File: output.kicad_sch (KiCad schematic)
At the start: 9 parts, among them Q3 NPN, Q4 PNP, U4 ${SIM.PARAMS}, U5 ${SIM.PARAMS}

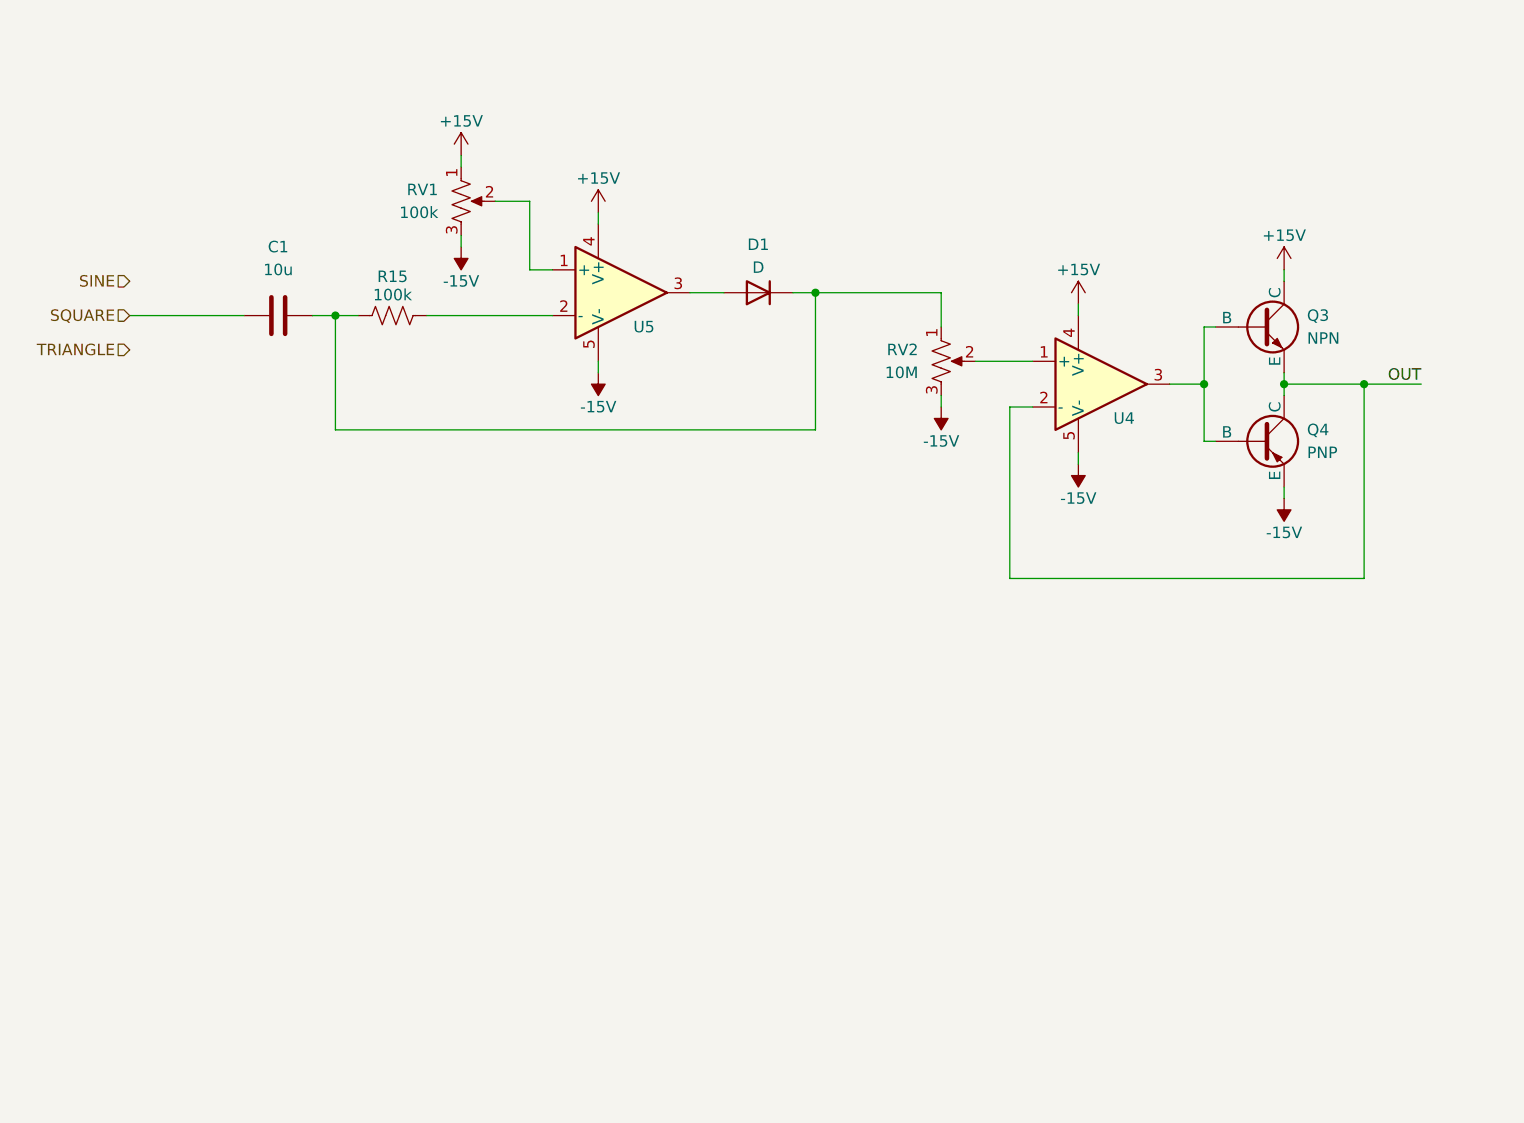
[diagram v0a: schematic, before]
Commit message: added spice model and reworked output stage
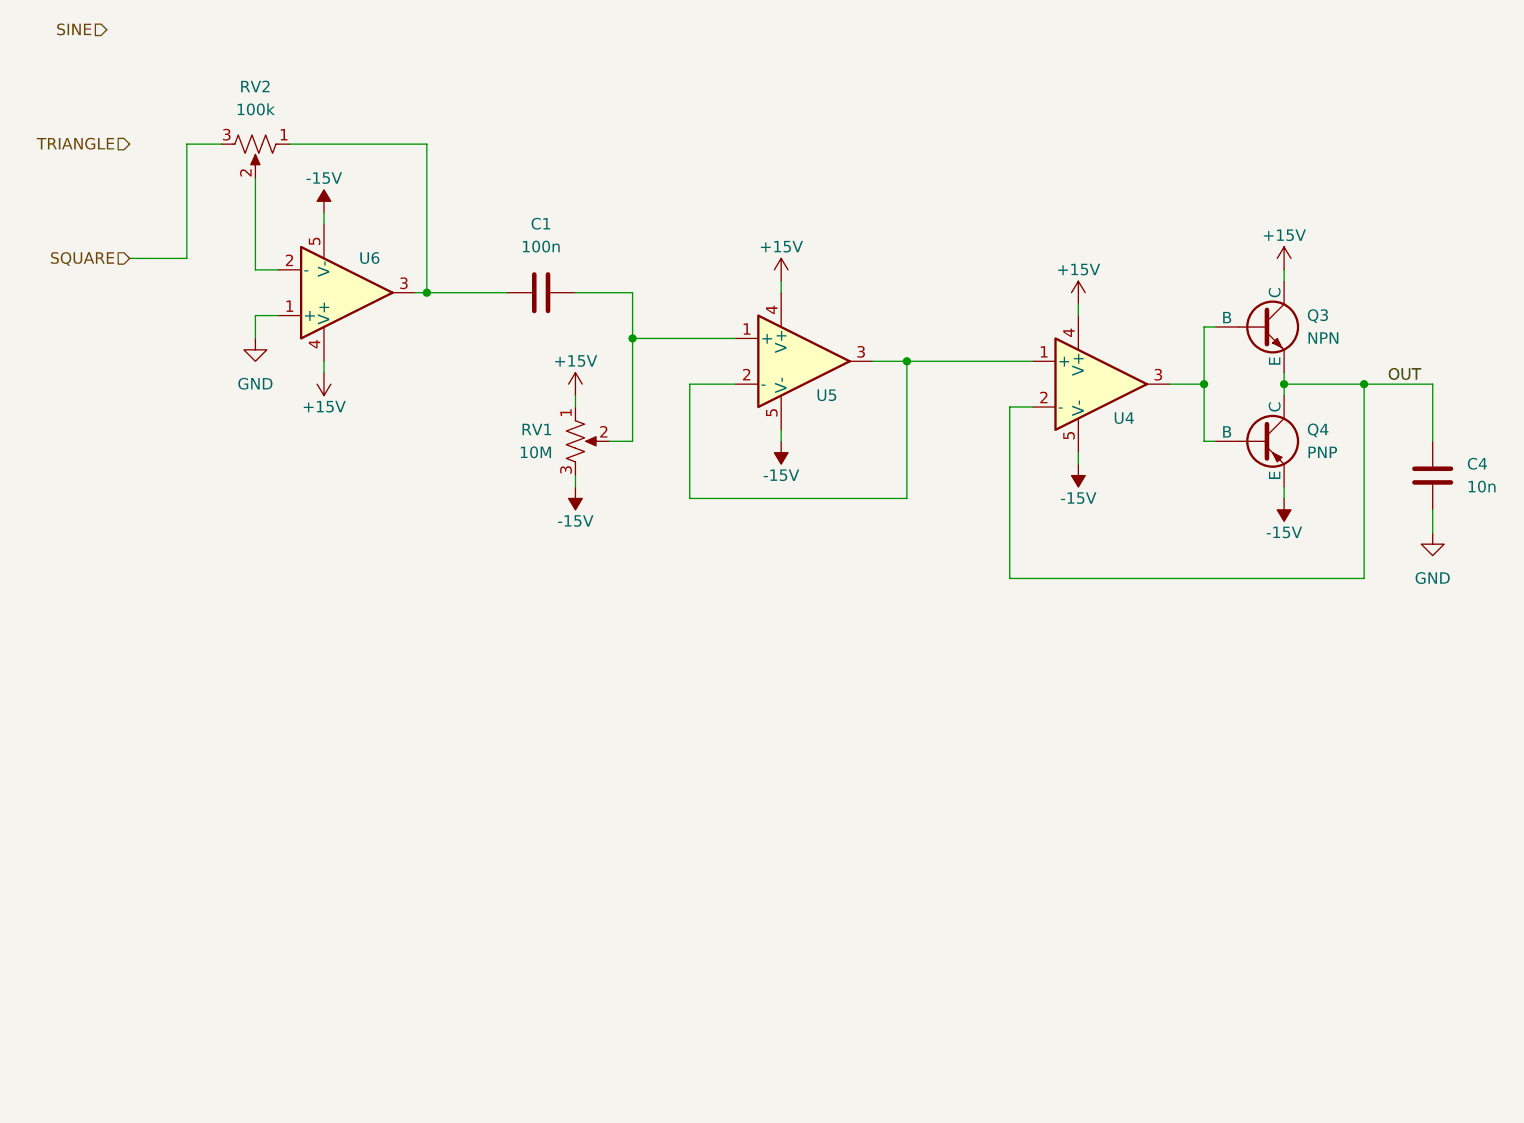
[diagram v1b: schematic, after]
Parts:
- removed D1: D, symbol Simulation_SPICE:D
- removed R15: 100k, symbol Device:R_US
- added C4: 10n, symbol Device:C
- added U6: ${SIM.PARAMS}, symbol Simulation_SPICE:OPAMP
- C1: value 10u -> 100n
- RV1: value 100k -> 10M
- RV2: value 10M -> 100k
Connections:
- net +15V: now also U6.4 (V+)
- net -15V: now also U6.5 (V-); no longer RV2.3
- net OUT: now also C4.1
- net SQUARE: now also RV2.3; no longer C1.1
- net at RV1.2, U5.1 (+): now also C1.2
- net at RV2.1: now also C1.1, U6.3; no longer C1.2
- net at RV2.2: now also U6.2 (-); no longer U4.1 (+)
- net at U5.3: now also U4.1 (+), U5.2 (-)
- new net GND: C4.2, U6.1 (+)
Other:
- moved on the sheet: C1

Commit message: added pulse gen and other stuff
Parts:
- removed U5: ${SIM.PARAMS}, symbol Simulation_SPICE:OPAMP
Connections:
- net at C1.2, RV1.2: now also U4.1 (+)
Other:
- moved on the sheet: C4, Q3, Q4, U4

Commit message: post wed changes
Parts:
- added C5: 100p, symbol Device:C
- added Q5, Q7: NPN, symbol Simulation_SPICE:NPN
- added Q6: PNP, symbol Simulation_SPICE:PNP
- added R18: 100, symbol Device:R_US
- added R19: 1k, symbol Device:R_US
- added R20: 10M, symbol Device:R_US
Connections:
- net +15V: now also Q5.1 (C), R18.1
- net -15V: now also Q4.1 (C); no longer Q4.3 (E)
- net GND: now also Q6.1 (C), Q7.3 (E), R20.2
- net OUT: now also Q4.3 (E); no longer Q4.1 (C)
- net PULSE: now also C5.1, R19.1
- new net: C5.2, Q7.2 (B), R19.2
- new net: Q5.2 (B), Q6.2 (B), Q7.1 (C), R18.2
- new net PULSE_OUT: Q5.3 (E), Q6.3 (E), R20.1
